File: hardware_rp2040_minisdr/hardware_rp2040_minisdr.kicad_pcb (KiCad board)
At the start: 2 copper layers, 67.8 x 20 mm, 51 parts, among them IC1 PSA4-5043+, IC2 ADE-11X+, IC3 SI5351A-B-GTR, IC4 GALI-84+, IC5 ADCS7476AIMFX_NOPB, J1 Conn_Coaxial_Small, J2 USB_A, SW1 SW_Push, U1 RP2040, U2 W25Q128JVS, U3 AMS1117-3.3, Y1 Crystal_GND24, Y2 Crystal_GND24

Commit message: pcb
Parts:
- moved IC1 116.7 mm to (203.5, 91.8), turned to -90 degrees
- moved C17 111.5 mm to (206.8, 94.8)
- moved SW1 91.5 mm to (167.7, 102.4)
- moved IC4 14.2 mm to (189.6, 96.5)
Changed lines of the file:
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@@
 	(footprint "Capacitor_SMD:C_0402_1005Metric"
 		(layer "F.Cu")
-		(at 99.93 62.76)
+		(at 206.77 94.75)
 		(descr "Capacitor SMD 0402 (1005 Metric), square (rectangular) end terminal, IPC-7351 nominal, (Body size source: IPC-SM-782 page 76, https://www.pcb-3d.com/wordpress/wp-content/uploads/ipc-sm-782a_amendment_1_and_2.pdf), generated with kicad-footprint-generator")
 		(tags "capacitor")
@@
 	(footprint "user_imported_devices:GALI5"
 		(layer "F.Cu")
-		(at 202.312 90.25 90)
+		(at 189.562 96.5 90)
 		(descr "DF782 (SOT-89 package)")
 		(tags "Integrated Circuit")
@@
 	(footprint "user_imported_devices:PSA45043"
 		(layer "F.Cu")
-		(at 86.815 90.71)
+		(at 203.5 91.75 -90)
 		(descr "PSA4-5043+-2")
 		(tags "Integrated Circuit")
 		(property "Reference" "IC1"
-			(at -0.113 0.012 0)
+			(at -0.113 0.012 90)
 			(layer "F.SilkS")
 			(effects
@@
 		)
 		(property "Value" "PSA4-5043+"
-			(at -0.113 0.012 0)
+			(at -0.113 0.012 90)
 			(layer "F.SilkS")
 			(hide yes)
@@
 		)
 		(property "Datasheet" "https://www.minicircuits.com/pdfs/PSA4-5043+.pdf"
-			(at 0 0 0)
+			(at 0 0 90)
 			(layer "F.Fab")
 			(hide yes)
@@
 		)
 		(property "Description" "Low Noise, High IP3 Monolithic Amplifier"
-			(at 0 0 0)
+			(at 0 0 90)
 			(layer "F.Fab")
 			(hide yes)
@@
 		)
 		(property "Height" "1.1"
-			(at 0 0 0)
+			(at 0 0 270)
 			(unlocked yes)
 			(layer "F.Fab")
@@
 		)
 		(property "Mouser Part Number" "139-PSA4-5043"
-			(at 0 0 0)
+			(at 0 0 270)
 			(unlocked yes)
 			(layer "F.Fab")
@@
 		)
 		(property "Mouser Price/Stock" "https://www.mouser.co.uk/ProductDetail/Mini-Circuits/PSA4-5043%2b?qs=xZ%2FP%252Ba9zWqbLkryIxS%2FdVA%3D%3D"
-			(at 0 0 0)
+			(at 0 0 270)
 			(unlocked yes)
 			(layer "F.Fab")
@@
 		)
 		(property "Manufacturer_Name" "Mini-Circuits"
-			(at 0 0 0)
+			(at 0 0 270)
 			(unlocked yes)
 			(layer "F.Fab")
@@
 		)
 		(property "Manufacturer_Part_Number" "PSA4-5043+"
-			(at 0 0 0)
+			(at 0 0 270)
 			(unlocked yes)
 			(layer "F.Fab")
@@
 		(attr smd)
 		(fp_line
-			(start -1.2 1.5)
-			(end -1.2 1.5)
+			(start -1.2 1.6)
+			(end -1.2 1.6)
 			(stroke
 				(width 0.1)
@@
 		)
 		(fp_line
-			(start -1.2 1.6)
-			(end -1.2 1.6)
+			(start -1.2 1.5)
+			(end -1.2 1.5)
 			(stroke
 				(width 0.1)
@@
 		)
 		(fp_arc
-			(start -1.2 1.5)
-			(mid -1.15 1.55)
-			(end -1.2 1.6)
+			(start -1.2 1.6)
+			(mid -1.25 1.55)
+			(end -1.2 1.5)
 			(stroke
 				(width 0.1)
@@
 		)
 		(fp_arc
-			(start -1.2 1.6)
-			(mid -1.25 1.55)
-			(end -1.2 1.5)
+			(start -1.2 1.5)
+			(mid -1.15 1.55)
+			(end -1.2 1.6)
 			(stroke
 				(width 0.1)
@@
 		)
 		(fp_line
-			(start -2.25 -2.575)
-			(end 2.025 -2.575)
+			(start -2.25 2.6)
+			(end -2.25 -2.575)
 			(stroke
 				(width 0.1)
@@
 		)
 		(fp_line
-			(start -2.25 2.6)
-			(end -2.25 -2.575)
+			(start 2.025 2.6)
+			(end -2.25 2.6)
 			(stroke
 				(width 0.1)
@@
 		)
 		(fp_line
-			(start 2.025 -2.575)
-			(end 2.025 2.6)
+			(start -2.25 -2.575)
+			(end 2.025 -2.575)
 			(stroke
 				(width 0.1)
@@
 		)
 		(fp_line
-			(start 2.025 2.6)
-			(end -2.25 2.6)
+			(start 2.025 -2.575)
+			(end 2.025 2.6)
 			(stroke
 				(width 0.1)
@@
 		)
 		(fp_line
-			(start -1.025 -0.625)
-			(end 1.025 -0.625)
+			(start -1.025 0.625)
+			(end -1.025 -0.625)
 			(stroke
 				(width 0.2)
@@
 		)
 		(fp_line
-			(start -1.025 0.625)
-			(end -1.025 -0.625)
+			(start 1.025 0.625)
+			(end -1.025 0.625)
 			(stroke
 				(width 0.2)
@@
 		)
 		(fp_line
-			(start 1.025 -0.625)
-			(end 1.025 0.625)
+			(start -1.025 -0.625)
+			(end 1.025 -0.625)
 			(stroke
 				(width 0.2)
@@
 		)
 		(fp_line
-			(start 1.025 0.625)
-			(end -1.025 0.625)
+			(start 1.025 -0.625)
+			(end 1.025 0.625)
 			(stroke
 				(width 0.2)
@@
 		)
 		(fp_text user "${REFERENCE}"
-			(at -0.113 0.012 0)
+			(at -0.113 0.012 90)
 			(layer "F.Fab")
 			(effects
@@
 		)
 		(pad "1" smd rect
-			(at -0.65 1.1)
+			(at -0.65 1.1 270)
 			(size 0.5 0.95)
 			(layers "F.Cu" "F.Mask" "F.Paste")
@@
 		)
 		(pad "2" smd rect
-			(at 0.5 1.1)
+			(at 0.5 1.1 270)
 			(size 0.8 0.95)
 			(layers "F.Cu" "F.Mask" "F.Paste")
@@
 		)
 		(pad "3" smd rect
-			(at 0.65 -1.1)
+			(at 0.65 -1.1 270)
 			(size 0.5 0.95)
 			(layers "F.Cu" "F.Mask" "F.Paste")
@@
 		)
 		(pad "4" smd rect
-			(at -0.65 -1.1)
+			(at -0.65 -1.1 270)
 			(size 0.5 0.95)
 			(layers "F.Cu" "F.Mask" "F.Paste")
@@
 	(footprint "Button_Switch_SMD:SW_SPST_PTS810"
 		(layer "F.Cu")
-		(at 76.87 90.98)
+		(at 167.675 102.425)
 		(descr "C&K Components, PTS 810 Series, Microminiature SMT Top Actuated, http://www.ckswitches.com/media/1476/pts810.pdf")
 		(tags "SPST Button Switch")

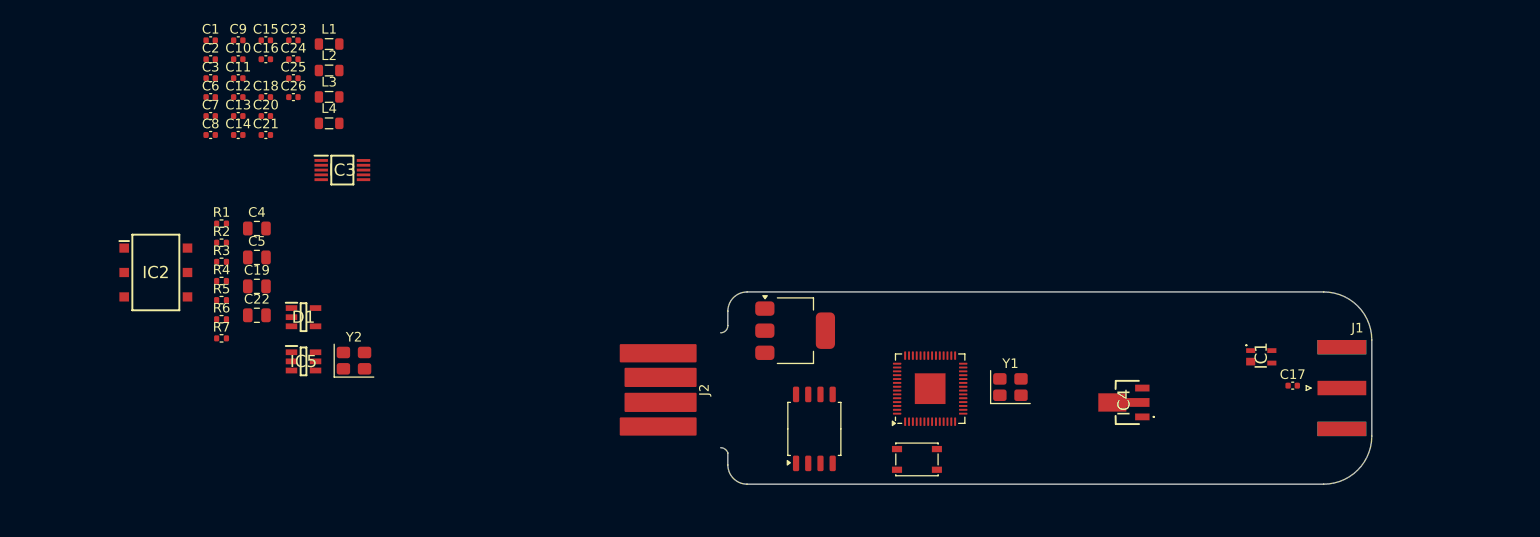
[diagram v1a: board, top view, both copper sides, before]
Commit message: pcb placement
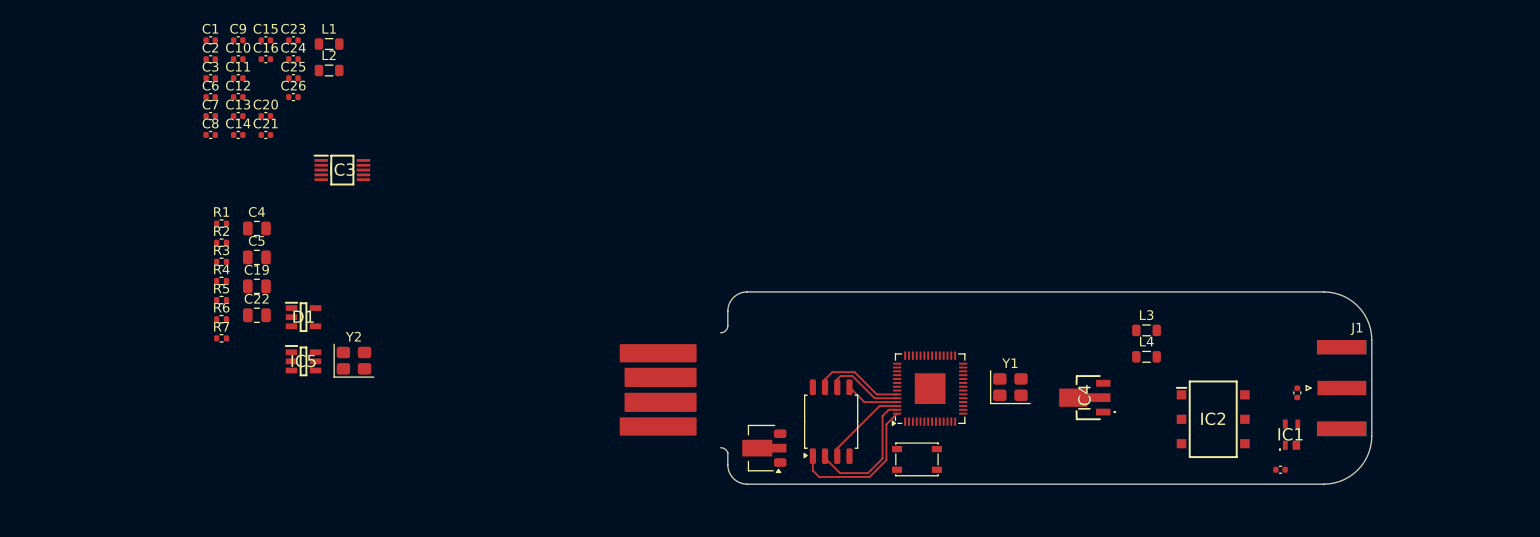
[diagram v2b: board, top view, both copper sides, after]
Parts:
- U3: value AMS1117-3.3 -> AMS1117S-3.3; footprint Package_TO_SOT_SMD:SOT-223-3_TabPin2 -> Package_TO_SOT_SMD:SOT-89-3
- moved C18 112.5 mm to (205.5, 103.5), turned to 180 degrees
- moved IC2 111.1 mm to (198.5, 98.2)
- moved L3 88.5 mm to (191.6, 89.0)
- moved L4 88.5 mm to (191.6, 91.8)
- moved U3 12.7 mm to (151.5, 101.2), turned to 180 degrees
- moved IC1 8.69 mm to (206.7, 99.8), turned to 0 degrees
- moved IC4 4.09 mm to (185.5, 96.0)
- moved U2 1.90 mm to (158.8, 98.5)
- moved C17 0.89 mm to (207.2, 95.5), turned to -90 degrees
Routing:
- net QSPI_SS: track 0.00 -> 15.5 mm
- net QSPI_SD1: track 0.00 -> 13.7 mm
- net QSPI_SD3: track 0.00 -> 9.58 mm
- net QSPI_SD2: track 0.00 -> 8.87 mm
- net QSPI_SCLK: track 0.00 -> 8.10 mm
- net QSPI_SD0: track 0.00 -> 5.60 mm
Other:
- copper layers 2 -> 4

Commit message: pcb
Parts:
- moved IC3 97.8 mm to (204.2, 89.0)
- moved Y2 87.3 mm to (196.4, 89.7)
- moved R5 72.6 mm to (166.0, 102.5), turned to 180 degrees
- moved SW1 5.83 mm to (173.5, 102.8)
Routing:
- net Net-(R5-Pad1): track 0.00 -> 9.62 mm
- net QSPI_SS: track 15.5 -> 16.4 mm
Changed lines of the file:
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@@
 	(footprint "Crystal:Crystal_SMD_3225-4Pin_3.2x2.5mm"
 		(layer "F.Cu")
-		(at 109.1 92.15)
+		(at 196.4 89.65)
 		(descr "SMD3225/4, Crystal, 3.2x2.5mm package, SMD, generated with kicad-footprint-generator make_crystal.py, http://www.txccrystal.com/images/pdf/7m-accuracy.pdf")
 		(property "Reference" "Y2"
 			(at 0 -2.45 0)
 			(layer "F.SilkS")
+			(hide yes)
 			(effects
 				(font
@@
 	(footprint "user_imported_devices:SI5351_SOP50P490X110-10N"
 		(layer "F.Cu")
-		(at 107.89 72.32)
+		(at 204.25 89)
 		(descr "10-MSOP Package")
 		(tags "Integrated Circuit")
@@
 	(footprint "Button_Switch_SMD:SW_SPST_PTS810"
 		(layer "F.Cu")
-		(at 167.675 102.425)
+		(at 173.5 102.75)
 		(descr "C&K Components, PTS 810 Series, Microminiature SMT Top Actuated, http://www.ckswitches.com/media/1476/pts810.pdf")
 		(tags "SPST Button Switch")
@@
 		)
 		(property "Value" "SW_Push"
-			(at 0 2.6 0)
+			(at 0 0 0)
 			(layer "F.Fab")
 			(effects
@@
 	(footprint "Resistor_SMD:R_0402_1005Metric"
 		(layer "F.Cu")
-		(at 95.32 85.85)
+		(at 165.99 102.5 180)
 		(descr "Resistor SMD 0402 (1005 Metric), square (rectangular) end terminal, IPC-7351 nominal, (Body size source: IPC-SM-782 page 72, https://www.pcb-3d.com/wordpress/wp-content/uploads/ipc-sm-782a_amendment_1_and_2.pdf), generated with kicad-footprint-generator")
 		(tags "resistor")
@@
 		(attr smd)
 		(fp_line
-			(start -0.153641 -0.38)
-			(end 0.153641 -0.38)
+			(start -0.153641 0.38)
+			(end 0.153641 0.38)
 			(stroke
 				(width 0.12)
@@
 		)
 		(fp_line
-			(start -0.153641 0.38)
-			(end 0.153641 0.38)
+			(start -0.153641 -0.38)
+			(end 0.153641 -0.38)
 			(stroke
 				(width 0.12)
@@
 		)
 		(fp_line
-			(start -0.93 -0.47)
-			(end 0.93 -0.47)
+			(start 0.93 0.47)
+			(end -0.93 0.47)
 			(stroke
 				(width 0.05)
@@
 		)
 		(fp_line
-			(start -0.93 0.47)
-			(end -0.93 -0.47)
+			(start 0.93 -0.47)
+			(end 0.93 0.47)
 			(stroke
 				(width 0.05)
@@
 		)
 		(fp_line
-			(start 0.93 -0.47)
-			(end 0.93 0.47)
+			(start -0.93 0.47)
+			(end -0.93 -0.47)
 			(stroke
 				(width 0.05)
@@
 		)
 		(fp_line
-			(start 0.93 0.47)
-			(end -0.93 0.47)
+			(start -0.93 -0.47)
+			(end 0.93 -0.47)
 			(stroke
 				(width 0.05)
@@
 		)
 		(fp_line
-			(start -0.525 -0.27)
-			(end 0.525 -0.27)
+			(start 0.525 0.27)
+			(end -0.525 0.27)
 			(stroke
 				(width 0.1)
@@
 		)
 		(fp_line
-			(start -0.525 0.27)
-			(end -0.525 -0.27)
+			(start 0.525 -0.27)
+			(end 0.525 0.27)
 			(stroke
 				(width 0.1)
@@
 		)
 		(fp_line
-			(start 0.525 -0.27)
-			(end 0.525 0.27)
+			(start -0.525 0.27)
+			(end -0.525 -0.27)
 			(stroke
 				(width 0.1)
@@
 		)
 		(fp_line
-			(start 0.525 0.27)
-			(end -0.525 0.27)
+			(start -0.525 -0.27)
+			(end 0.525 -0.27)
 			(stroke
 				(width 0.1)
@@
 		)
 		(pad "1" smd roundrect
-			(at -0.51 0)
+			(at -0.51 0 180)
 			(size 0.54 0.64)
 			(layers "F.Cu" "F.Mask" "F.Paste")
@@
 		)
 		(pad "2" smd roundrect
-			(at 0.51 0)
+			(at 0.51 0 180)
 			(size 0.54 0.64)
 			(layers "F.Cu" "F.Mask" "F.Paste")
@@
 	)
 	(segment
+		(start 166.5 102.5)
+		(end 170.1 102.5)
+		(width 0.2)
+		(layer "F.Cu")
+		(net 36)
+	)
+	(segment
+		(start 170.1 102.5)
+		(end 171.425 103.825)
+		(width 0.2)
+		(layer "F.Cu")
+		(net 36)
+	)
+	(segment
+		(start 171.425 103.825)
+		(end 175.575 103.825)
+		(width 0.2)
+		(layer "F.Cu")
+		(net 36)
+	)
+	(segment
 		(start 164.5 102.5)
 		(end 162.75 104.25)
@@
 		(width 0.2)
 		(layer "F.Cu")
+		(net 37)
+	)
+	(segment
+		(start 164.5 102.5)
+		(end 165.48 102.5)
+		(width 0.2)
+		(layer "F.Cu")

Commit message: pcb
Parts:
- moved C21 95.3 mm to (189.8, 100.5), turned to 90 degrees
- moved R4 80.8 mm to (175.2, 96.2), turned to 180 degrees
- moved C14 72.4 mm to (166.5, 89.3), turned to 90 degrees
- moved C10 71.3 mm to (165.7, 80.1)
- moved C11 71.3 mm to (165.7, 82.1)
- moved C12 71.3 mm to (165.7, 84.0)
- moved C15 71.3 mm to (168.6, 78.1)
- moved C9 71.3 mm to (165.7, 78.1)
- moved C13 69.7 mm to (162.2, 91.2)
- moved Y2 2.41 mm to (196.7, 87.2), turned to 90 degrees
- moved Y1 2.37 mm to (178.2, 97.2), turned to -90 degrees
- moved IC2 2.14 mm to (200.2, 99.5)
- moved IC3 1.60 mm to (203.2, 87.8)
- moved IC4 1.05 mm to (185.8, 95.0)
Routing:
- net Net-(IC3-XA): track 0.00 -> 5.71 mm
- net Net-(IC3-XB): track 0.00 -> 3.80 mm
- net Net-(U1-XIN): track 0.00 -> 3.11 mm
- net GND: track 0.00 -> 2.44 mm
- net Net-(C2-Pad1): track 0.00 -> 1.68 mm
- net (no net): vias 0 -> 2

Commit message: pcb
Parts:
- moved C23 109.5 mm to (209.2, 84.8)
- moved C24 107.8 mm to (209.1, 79.2)
- moved C19 106.0 mm to (203.6, 101.3), turned to -90 degrees
- moved L1 103.0 mm to (200.1, 102.3), turned to 180 degrees
- moved C20 101.6 mm to (198.8, 90.3), turned to 180 degrees
- moved R6 92.7 mm to (188.0, 91.0), turned to 90 degrees
- moved C3 92.0 mm to (178.3, 100.0)
- moved C2 90.8 mm to (178.5, 94.5)
- moved C1 90.1 mm to (179.0, 89.2), turned to -90 degrees
- moved C25 89.8 mm to (184.8, 99.5)
- moved C22 89.0 mm to (188.0, 88.8)
- moved L2 88.1 mm to (189.0, 93.0), turned to 180 degrees
- moved R7 87.4 mm to (182.8, 91.5), turned to 180 degrees
- moved C7 86.5 mm to (176.2, 94.2)
- moved R1 84.8 mm to (179.0, 91.5), turned to 180 degrees
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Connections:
- C20 pad 1: Net-(IC3-CLK0) -> Net-(IC3-CLK2)
- IC3 pad 10: Net-(IC3-CLK0) -> unconnected-(IC3-CLK0-Pad10)
- IC3 pad 6: unconnected-(IC3-CLK2-Pad6) -> Net-(IC3-CLK2)
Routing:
- net 3v3: track 0.00 -> 29.1 mm, vias 0 -> 2
- net VBUS: track 0.00 -> 26.2 mm, vias 0 -> 4
- net USB_DN: track 0.00 -> 23.2 mm, vias 0 -> 2
- net USB_DP: track 0.00 -> 21.5 mm
- net QSPI_SS: track 16.4 -> 0.81 mm
- net QSPI_SD1: track 13.7 -> 0.60 mm
- net QSPI_SD3: track 9.58 -> 0.00 mm
- net QSPI_SD2: track 8.87 -> 0.00 mm
- net QSPI_SCLK: track 8.10 -> 0.20 mm
- net 1v1: track 0.00 -> 7.58 mm
- net Net-(U1-XIN): track 3.11 -> 9.64 mm
- net QSPI_SD0: track 5.60 -> 0.00 mm
- net GND: track 2.44 -> 7.72 mm, vias 0 -> 2
- net Net-(U1-USB_DM): track 0.00 -> 3.83 mm
- net Net-(U1-USB_DP): track 0.00 -> 3.59 mm
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
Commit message: pcb
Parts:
- moved C23 7.71 mm to (201.8, 82.6), turned to -90 degrees
- moved IC3 6.02 mm to (205.0, 76.0), turned to 90 degrees
- moved Y2 4.69 mm to (204.5, 82.6), turned to 180 degrees
- moved C24 3.72 mm to (207.2, 82.5), turned to -90 degrees

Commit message: pcb
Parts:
- moved IC3 12.9 mm to (200.9, 88.2), turned to 180 degrees
- moved C23 10.9 mm to (206.8, 92.2), turned to 0 degrees
- moved Y2 7.26 mm to (206.8, 89.5), turned to -90 degrees
- moved C24 4.29 mm to (206.7, 86.8), turned to 0 degrees
- moved C21 1.06 mm to (191.2, 94.5)
- moved C22 1.06 mm to (187.2, 89.5)
- moved L2 1.06 mm to (188.2, 93.8)
- moved R6 1.06 mm to (187.2, 91.8)
- moved IC2 1.05 mm to (189.5, 100.0)
- moved C20 0.98 mm to (198.2, 91.0)
- moved IC4 0.98 mm to (193.8, 89.5)
- moved C4 0.80 mm to (158.2, 90.5)
- moved C25 0.79 mm to (184.0, 99.2)
- moved C17 0.78 mm to (198.8, 95.5)
- moved C12 0.75 mm to (161.7, 93.8)
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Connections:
- C20 pad 1: Net-(IC3-CLK2) -> Net-(IC3-CLK0)
- IC3 pad 10: unconnected-(IC3-CLK0-Pad10) -> Net-(IC3-CLK0)
- IC3 pad 6: Net-(IC3-CLK2) -> unconnected-(IC3-CLK2-Pad6)
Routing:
- net SCL: track 0.00 -> 34.9 mm
- net SDA: track 0.00 -> 31.3 mm
- net ADC_MISO: track 1.81 -> 22.8 mm
- net ADC_CS: track 2.21 -> 20.5 mm
- net QSPI_SS: track 0.81 -> 18.3 mm
- net ADC_SCLK: track 1.85 -> 18.1 mm
- net 3v3: track 29.1 -> 44.2 mm
- net QSPI_SD1: track 0.60 -> 15.3 mm
- net Net-(IC5-VIN): track 0.00 -> 13.2 mm
- net Net-(J1-In): track 0.00 -> 13.1 mm
- net Net-(IC4-RF-OUT_&_DC-IN): track 0.00 -> 13.0 mm
- net QSPI_SD3: track 0.00 -> 13.0 mm
- net QSPI_SD2: track 0.00 -> 12.6 mm
- net QSPI_SCLK: track 0.20 -> 11.7 mm
- net Net-(IC2-RF): track 0.00 -> 11.4 mm
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
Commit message: pcb hardware!
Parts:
- J2: footprint user_imported_devices:USBPCB -> Connector_USB:USB_A_Connfly_DS1098_Horizontal
- moved J2 9.20 mm to (135.6, 95.4), turned to 180 degrees
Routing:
- net GND: track 11.6 -> 101.4 mm, vias 9 -> 71
- net VBUS: track 31.3 -> 82.4 mm, vias 4 -> 8
- net 3v3: track 44.2 -> 58.1 mm, vias 2 -> 9
- net 1v1: track 15.1 -> 27.4 mm, vias 0 -> 2
- net USB_DP: track 22.3 -> 16.9 mm
- net USB_DN: track 23.6 -> 18.5 mm
- net SDA: track 31.3 -> 33.1 mm
- net Net-(IC3-XA): track 5.27 -> 7.07 mm
- net Net-(IC3-XB): track 2.86 -> 4.62 mm
- net Net-(IC5-VIN): track 13.2 -> 15.0 mm
- net Net-(IC1-RF-OUT_&_DC-IN): track 2.56 -> 4.27 mm
- net SCL: track 34.9 -> 36.3 mm
- net ADC_CS: track 20.5 -> 21.8 mm
- net ADC_MISO: track 22.8 -> 24.1 mm
- net ADC_SCLK: track 18.1 -> 19.3 mm
- added copper zone on In2.Cu, net 3v3
- added copper zone on B.Cu, net GND
- added copper zone on F.Cu, net GND
- added copper zone on In1.Cu, net GND
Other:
- board size 67.8 x 20 mm -> 74.2 x 20 mm
